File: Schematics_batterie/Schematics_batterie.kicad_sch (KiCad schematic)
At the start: 4 parts

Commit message: ya
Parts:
- added U2: MCP1802x-xx02xOT, Package_TO_SOT_SMD:SOT-23-5, symbol Regulator_Linear:MCP1802x-xx02xOT
- added U3: STM32G431KBTx, Package_QFP:LQFP-32_7x7mm_P0.8mm, symbol MCU_ST_STM32G4:STM32G431KBTx
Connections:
- new net: U3.16 (VSS), U3.32 (VSS)
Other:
- note added: "MCU"
- note added: "Regulateur MCU"
- company: (none) -> ENSEA
- title: (none) -> PCB : Batterie Veste Lumineuse

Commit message: ok
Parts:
- removed U1: ~, symbol SamacSys_Parts:595-BQ25185DLHR
- removed U2: MCP1802x-xx02xOT, Package_TO_SOT_SMD:SOT-23-5, symbol Regulator_Linear:MCP1802x-xx02xOT
- added C4, C5: 1 µ, Capacitor_SMD:C_0603_1608Metric_Pad1.08x0.95mm_HandSolder, symbol Device:C_Small
- added IC1: BQ25185DLHR, SON40P220X200X80-11N, symbol BQ25185DLHR:BQ25185DLHR
- added U1: BU33SD5WG-TR, Package_TO_SOT_SMD:SOT-23-5, symbol Regulator_Linear:MCP1802x-xx02xOT
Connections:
- net BAT: now also C3.2, IC1.2 (BAT); no longer C3.1
- net Charge Enabler: now also IC1.4 (~{CE})
- net DC Input: now also IC1.10 (IN)
- net GND: now also C3.1, C4.2, C5.2, IC1.5 (GND), U1.2 (GND); no longer C3.2
- net STAT1: now also IC1.9 (STAT1)
- net STAT2: now also IC1.3 (STAT2)
- net SYS: now also IC1.1 (SYS)
- new net +3.3V: C5.1, U1.5 (VOUT)
- new net +5V: C4.1, U1.1 (VIN), U1.3 (~{SHDN})
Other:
- moved on the sheet: C1, C3

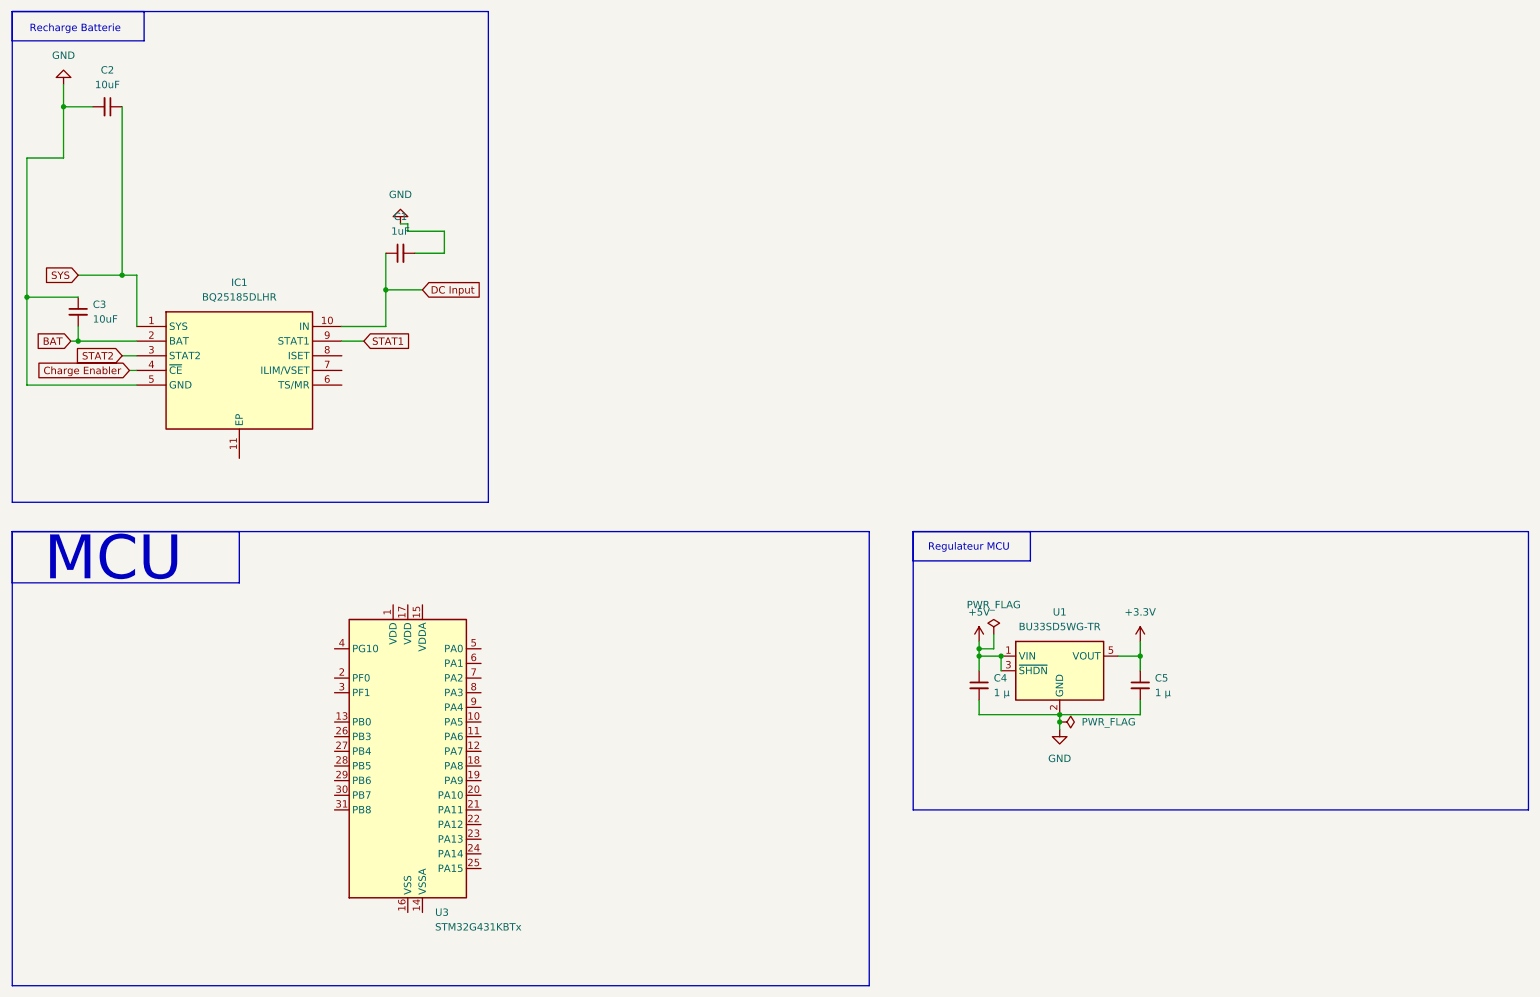
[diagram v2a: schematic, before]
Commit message: version avec usbc
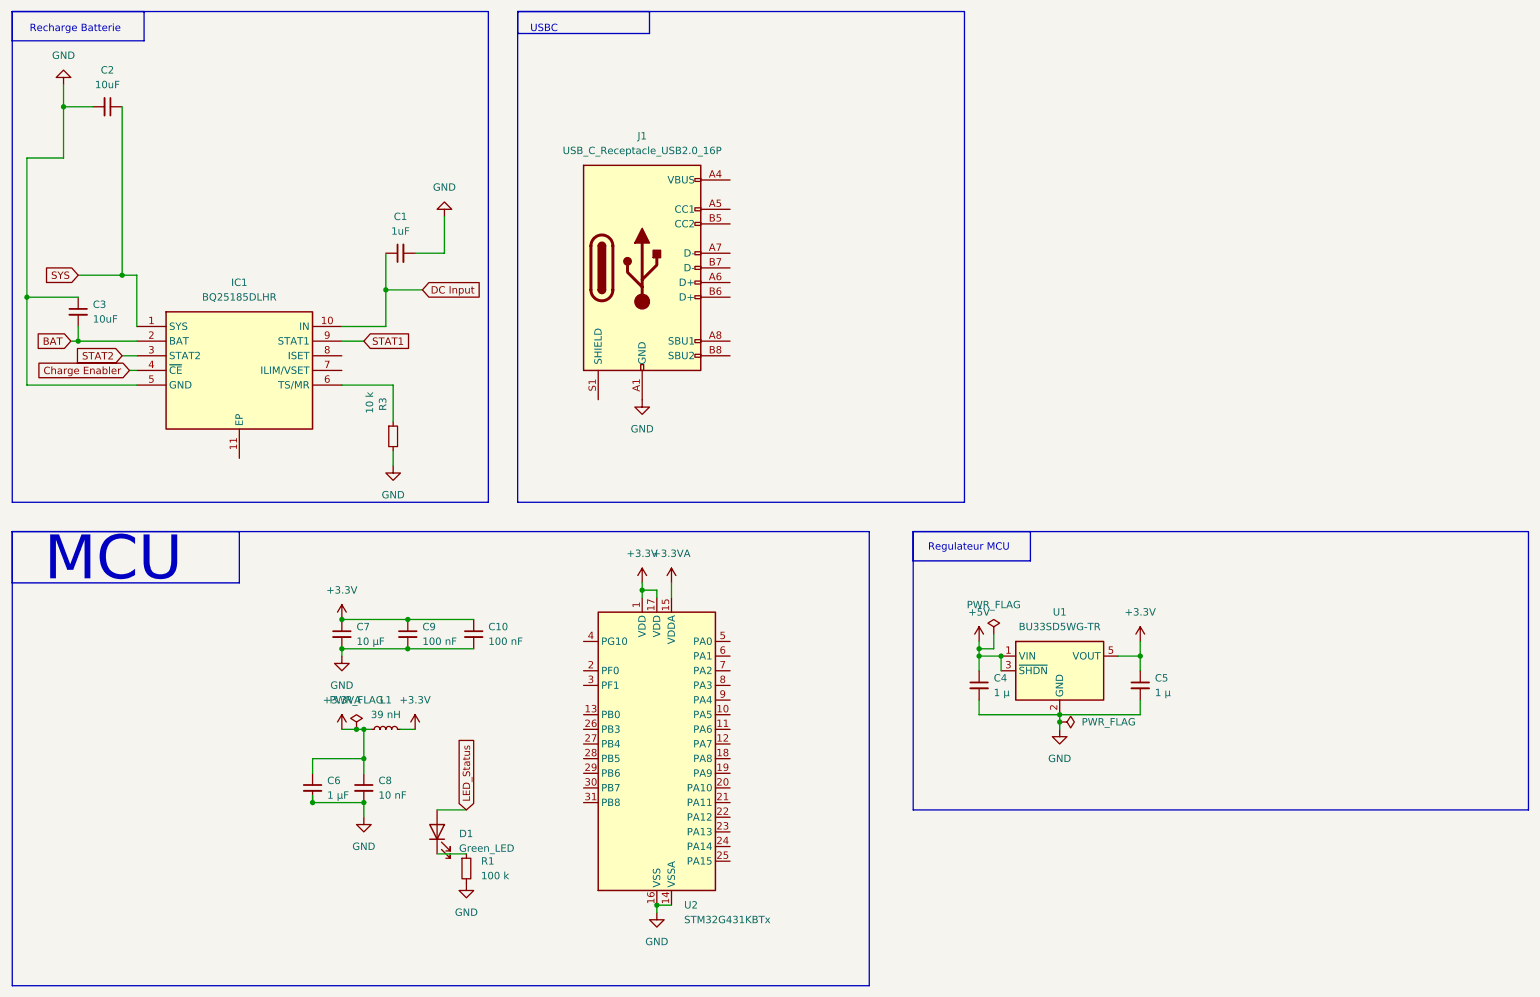
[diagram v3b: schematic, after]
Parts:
- removed U3: STM32G431KBTx, Package_QFP:LQFP-32_7x7mm_P0.8mm, symbol MCU_ST_STM32G4:STM32G431KBTx
- added C10, C9: 100 nF, Capacitor_SMD:C_0603_1608Metric_Pad1.08x0.95mm_HandSolder, symbol Device:C_Small
- added C6: 1 µF, Capacitor_SMD:C_0603_1608Metric_Pad1.08x0.95mm_HandSolder, symbol Device:C_Small
- added C7: 10 µF, Capacitor_SMD:C_0603_1608Metric_Pad1.08x0.95mm_HandSolder, symbol Device:C_Small
- added C8: 10 nF, Capacitor_SMD:C_0603_1608Metric_Pad1.08x0.95mm_HandSolder, symbol Device:C_Small
- added D1: Green_LED, LED_SMD:LED_0603_1608Metric_Pad1.05x0.95mm_HandSolder, symbol Device:LED
- added J1: USB_C_Receptacle_USB2.0_16P, symbol Connector:USB_C_Receptacle_USB2.0_16P
- added L1: 39 nH, Inductor_SMD:L_0603_1608Metric_Pad1.05x0.95mm_HandSolder, symbol Device:L_Small
- added R1: 100 k, Resistor_SMD:R_0603_1608Metric_Pad0.98x0.95mm_HandSolder, symbol Device:R_Small
- added R3: 10 k, symbol Device:R_Small
- added U2: STM32G431KBTx, Package_QFP:LQFP-32_7x7mm_P0.8mm, symbol MCU_ST_STM32G4:STM32G431KBTx
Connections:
- net +3.3V: now also C10.1, C7.1, C9.1, L1.2, U2.1 (VDD), U2.17 (VDD)
- net GND: now also C10.2, C6.2, C7.2, C8.2, C9.2, J1.A1 (GND), J1.A12 (GND), J1.B1 (GND), J1.B12 (GND), R1.2, R3.2, U2.14 (VSSA), U2.16 (VSS), U2.32 (VSS)
- net at IC1.6 (TS/MR): now also R3.1
- new net: D1.1 (K), R1.1
- new net: J1.A4 (VBUS), J1.A9 (VBUS), J1.B4 (VBUS), J1.B9 (VBUS)
- new net +3.3VA: C6.1, C8.1, L1.1, U2.15 (VDDA)
- new net LED_Status: D1.2 (A)
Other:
- note added: "USBC"

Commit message: ya
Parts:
- IC1: footprint SON40P220X200X80-11N -> (none)
- J1: footprint (none) -> Connector_USB:USB_C_Receptacle_HCTL_HC-TYPE-C-16P-01A
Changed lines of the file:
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@@
 			)
 		)
-		(property "Footprint" "SON40P220X200X80-11N"
+		(property "Footprint" ""
 			(at 73.66 172.39 0)
 			(effects
@@
 			)
 		)
-		(property "Footprint" ""
+		(property "Footprint" "Connector_USB:USB_C_Receptacle_HCTL_HC-TYPE-C-16P-01A"
 			(at 133.35 67.31 0)
 			(effects

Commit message: newé
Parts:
- added C11: 100uF, symbol Device:C_Small
- added J2: Conn_02x07_Odd_Even, Connector_PinHeader_1.27mm:PinHeader_2x07_P1.27mm_Vertical_SMD, symbol Connector_Generic:Conn_02x07_Odd_Even
- added J3: Conn_01x02, Connector_JST:JST_XH_B2B-XH-A_1x02_P2.50mm_Vertical, symbol Connector_Generic:Conn_01x02
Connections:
- net +3.3V: now also J2.3 (Pin_3)
- net +5V: now also J3.1 (Pin_1)
- net GND: now also C11.1, J2.5 (Pin_5), J2.7 (Pin_7), J3.2 (Pin_2)
- net SYS_SWDIO: now reaches U2.23 (PA13)
- net SYS_SWDIO: now also J2.4 (Pin_4)
- net SYS_SWCLK: now reaches U2.24 (PA14)
- net SYS_SWCLK: now also J2.6 (Pin_6)
- net NRST: now reaches U2.4 (PG10)
- net NRST: now also C11.2, J2.12 (Pin_12)
- net USART2_TX: now reaches U2.7 (PA2)
- net USART2_TX: now also J2.14 (Pin_14)
- net USART2_RX: now reaches U2.8 (PA3)
- net USART2_RX: now also J2.13 (Pin_13)
- no-connect marks 0 -> 6
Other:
- note added: "Connecteurs"
- note added: "Programmeur"
- moved on the sheet: C10, C6, C7, C8, C9, D1, L1, R1, U2

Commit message: yep
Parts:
- added R2, R4: R_Small, symbol Device:R_Small
- added U3: USBLC6-2SC6, Package_TO_SOT_SMD:SOT-23-6, symbol Power_Protection:USBLC6-2SC6
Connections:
- net GND: now also IC1.11 (EP), R2.2, R4.1, U3.2 (GND)
- net at J1.A5 (CC1): now also R2.1
- net at J1.B5 (CC2): now also R4.2
